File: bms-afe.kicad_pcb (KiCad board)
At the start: 0 parts

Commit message: started layout
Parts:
- added C11: CAP CER 1000PF 50V X7R 0603, Capacitor_SMD:C_0603_1608Metric, F.Cu at (121.5, 115.4)
- added C12: CAP CER 1000PF 50V X7R 0603, Capacitor_SMD:C_0603_1608Metric, F.Cu at (149.8, 106.7)
- added C13: CAP CER 1000PF 50V X7R 0603, Capacitor_SMD:C_0603_1608Metric, F.Cu at (121.5, 117.9)
- added C14: CAP CER 250PF 25V NP0 0603, Capacitor_SMD:C_0603_1608Metric, F.Cu at (203.0, 42.0)
- added C15: CAP CER 0603 1NF 16V X7R 10%, Capacitor_SMD:C_0603_1608Metric, F.Cu at (200.5, 45.0)
- added C16: CAP CER 220PF 50V X7R 0603, Capacitor_SMD:C_0603_1608Metric, F.Cu at (202.5, 45.0)
- added C17: CAP CER 0603 1NF 16V X7R 10%, Capacitor_SMD:C_0603_1608Metric, F.Cu at (208.0, 41.5)
- added C18: 4.7nF, Capacitor_SMD:C_0603_1608Metric, F.Cu at (166.1, 39.8)
- added C19: CAP CER 220PF 50V X7R 0603, Capacitor_SMD:C_0603_1608Metric, F.Cu at (210.0, 41.5)
- added C20: 4.7nF, Capacitor_SMD:C_0603_1608Metric, F.Cu at (166.1, 44.8)
- added C21: 4.7nF, Capacitor_SMD:C_0603_1608Metric, F.Cu at (170.1, 29.8)
- added C22: 1000pF, Capacitor_SMD:C_0603_1608Metric, F.Cu at (170.1, 32.3)
- added C23: CAP CER 220PF 50V X7R 0603, Capacitor_SMD:C_0603_1608Metric, F.Cu at (198.5, 48.0)
- added C24: CAP CER 0603 1NF 16V X7R 10%, Capacitor_SMD:C_0603_1608Metric, F.Cu at (196.5, 48.0)
- added C25: 10nF, Capacitor_SMD:C_0603_1608Metric, F.Cu at (170.1, 39.8)
- added C26: CAP CER 1000PF 50V X7R 0603, Capacitor_SMD:C_0603_1608Metric, F.Cu at (165.0, 76.8)
- added C27: CAP CER 220PF 50V X7R 0603, Capacitor_SMD:C_0603_1608Metric, F.Cu at (194.0, 46.0)
- added C28: CAP CER 0603 1NF 16V X7R 10%, Capacitor_SMD:C_0603_1608Metric, F.Cu at (194.0, 44.0)
- added C29: 10nF, Capacitor_SMD:C_0603_1608Metric, F.Cu at (174.1, 29.8)
- added C30: 10nF, Capacitor_SMD:C_0603_1608Metric, F.Cu at (174.1, 32.3)
- added C31: CAP CER 1000PF 50V X7R 0603, Capacitor_SMD:C_0603_1608Metric, F.Cu at (149.8, 76.8)
- added C32: CAP CER 1000PF 50V X7R 0603, Capacitor_SMD:C_0603_1608Metric, F.Cu at (149.8, 121.6)
- added C33: CAP CER 1000PF 50V X7R 0603, Capacitor_SMD:C_0603_1608Metric, F.Cu at (149.8, 91.7)
- added C34: CAP CER 1000PF 50V X7R 0603, Capacitor_SMD:C_0603_1608Metric, F.Cu at (165.0, 91.7)
- added C35: CAP CER 0.1UF 25V X7R 0603, Capacitor_SMD:C_0603_1608Metric, F.Cu at (149.8, 109.2)
- added C37: CAP CER 0.1UF 25V X7R 0603, Capacitor_SMD:C_0603_1608Metric, F.Cu at (165.0, 79.3)
- added C39: CAP CER 0.1UF 25V X7R 0603, Capacitor_SMD:C_0603_1608Metric, F.Cu at (149.8, 79.3)
- added C41: CAP CER 0.1UF 25V X7R 0603, Capacitor_SMD:C_0603_1608Metric, F.Cu at (149.8, 124.1)
- added C42: CAP CER 0.1UF 25V X7R 0603, Capacitor_SMD:C_0603_1608Metric, F.Cu at (149.8, 94.2)
- added C43: CAP CER 0.1UF 25V X7R 0603, Capacitor_SMD:C_0603_1608Metric, F.Cu at (165.0, 94.2)
- added C44: 0.1uF, Capacitor_SMD:C_0603_1608Metric, F.Cu at (203.0, 34.0)
- added C45: 0.1uF, Capacitor_SMD:C_0603_1608Metric, F.Cu at (203.0, 38.0)
- added C46: 0.1uF, Capacitor_SMD:C_0603_1608Metric, F.Cu at (203.0, 36.0)
- added C47: 0.1uF, Capacitor_SMD:C_0603_1608Metric, F.Cu at (186.0, 47.5)
- added C54: CAP CER 0.33UF 16V X7R 0603, Capacitor_SMD:C_0603_1608Metric, F.Cu at (121.5, 120.5)
- added C55: CAP CER 0.33UF 16V X7R 0603, Capacitor_SMD:C_0603_1608Metric, F.Cu at (121.5, 123.0)
- added C56: CAP CER 0.33UF 16V X7R 0603, Capacitor_SMD:C_0603_1608Metric, F.Cu at (125.5, 115.4)
- added C57: CAP CER 0.33UF 16V X7R 0603, Capacitor_SMD:C_0603_1608Metric, F.Cu at (125.5, 117.9)
- added C58: CAP CER 0.33UF 16V X7R 0603, Capacitor_SMD:C_0603_1608Metric, F.Cu at (125.5, 120.5)
- added C59: CAP CER 0.33UF 16V X7R 0603, Capacitor_SMD:C_0603_1608Metric, F.Cu at (125.5, 123.0)
- added C60: CAP CER 0.33UF 25V X7R 0603, Capacitor_SMD:C_0603_1608Metric, F.Cu at (129.5, 115.4)
- added D1: 1.6X0.8MM RED/WHT SMD LED, Diode_SMD:D_0603_1608Metric, F.Cu at (159.0, 115.2)
- added D2: 1.6X0.8MM RED/WHT SMD LED, Diode_SMD:D_0603_1608Metric, F.Cu at (174.2, 85.3)
- added D3: 1.6X0.8MM RED/WHT SMD LED, Diode_SMD:D_0603_1608Metric, F.Cu at (159.0, 85.3)
- added D4: 1.6X0.8MM RED/WHT SMD LED, Diode_SMD:D_0603_1608Metric, F.Cu at (159.0, 130.1)
- added D5: 1.6X0.8MM RED/WHT SMD LED, Diode_SMD:D_0603_1608Metric, F.Cu at (159.0, 100.2)
- added D6: 1.6X0.8MM RED/WHT SMD LED, Diode_SMD:D_0603_1608Metric, F.Cu at (174.2, 100.2)
- added GSF1: MOSFET, P-CH, SINGLE, -4.1A, -30, Package_TO_SOT_SMD:SOT-23-3, F.Cu at (154.4, 116.1)
- added GSF2: MOSFET, P-CH, SINGLE, -4.1A, -30, Package_TO_SOT_SMD:SOT-23-3, F.Cu at (169.6, 86.2)
- added GSF3: MOSFET, P-CH, SINGLE, -4.1A, -30, Package_TO_SOT_SMD:SOT-23-3, F.Cu at (154.4, 86.2)
- added GSF4: MOSFET, P-CH, SINGLE, -4.1A, -30, Package_TO_SOT_SMD:SOT-23-3, F.Cu at (154.4, 131.1)
- added GSF5: MOSFET, P-CH, SINGLE, -4.1A, -30, Package_TO_SOT_SMD:SOT-23-3, F.Cu at (154.4, 101.2)
- added GSF6: MOSFET, P-CH, SINGLE, -4.1A, -30, Package_TO_SOT_SMD:SOT-23-3, F.Cu at (169.6, 101.2)
- added J1: CONN HEADER VERT 7POS 2.5MM, footprints:JST_B7B-XH-A_LF__SN_, F.Cu at (71.0, 99.5)
- added J2: CONN HEADER VERT 2POS 1.5MM, footprints:CONN_B2B-ZR_02P_JST, F.Cu at (191.0, 89.5)
- added J3: CONN HEADER VERT 2POS 1.5MM, footprints:CONN_B2B-ZR_02P_JST, F.Cu at (207.0, 87.5)
- added J4: CONN HEADER VERT 6POS 1.5MM, footprints:CONN_B6B-ZR_JST, F.Cu at (168.6, 49.1)
- added R1: RES 10 OHM 1% 1/10W 0603, Resistor_SMD:R_0603_1608Metric, F.Cu at (129.5, 117.9)
- added R10: RES SMD 52.3 OHM 1% 1/2W 1210, Capacitor_SMD:C_1210_3225Metric, F.Cu at (169.9, 77.6)
- added R11: RES SMD 52.3 OHM 1% 1/2W 1210, Capacitor_SMD:C_1210_3225Metric, F.Cu at (169.9, 81.9)
- added R12: RES SMD 8.2 OHM 1% 1/8W 0603, Capacitor_SMD:C_0603_1608Metric, F.Cu at (165.0, 81.8)
- added R13: RES 10 OHM 1% 1/10W 0603, Resistor_SMD:R_0603_1608Metric, F.Cu at (165.0, 84.3)
- added R14: RES 100 OHM 1% 1/10W 0603, Resistor_SMD:R_0603_1608Metric, F.Cu at (200.5, 41.5)
- added R15: 100, Resistor_SMD:R_0603_1608Metric, F.Cu at (203.0, 40.0)
- added R16: 20k, Capacitor_SMD:C_0603_1608Metric, F.Cu at (216.0, 38.5)
- added R17: 20k, Capacitor_SMD:C_0603_1608Metric, F.Cu at (216.0, 41.0)
- added R18: RES SMD 39 OHM 5% 1/8W 0603, Resistor_SMD:R_0603_1608Metric, F.Cu at (198.5, 43.0)
- added R19: 20k, Capacitor_SMD:C_0603_1608Metric, F.Cu at (178.1, 39.8)
- added R2: RES 10 OHM 1% 1/10W 0603, Resistor_SMD:R_0603_1608Metric, F.Cu at (129.5, 120.5)
- added R20: 20k, Capacitor_SMD:C_0603_1608Metric, F.Cu at (178.1, 42.3)
- added R21: RES SMD 39 OHM 5% 1/8W 0603, Resistor_SMD:R_0603_1608Metric, F.Cu at (206.0, 40.0)
- added R22: RES 100 OHM 1% 1/10W 0603, Resistor_SMD:R_0603_1608Metric, F.Cu at (182.1, 29.8)
- added R23: RES SMD 10K OHM 1% 1/8W 0603, Resistor_SMD:R_0603_1608Metric, F.Cu at (182.1, 32.3)
- added R24: RES SMD 39 OHM 5% 1/8W 0603, Resistor_SMD:R_0603_1608Metric, F.Cu at (198.0, 45.5)
- added R25: RES SMD 10K OHM 1% 1/8W 0603, Resistor_SMD:R_0603_1608Metric, F.Cu at (182.1, 37.3)
- added R26: RES SMD 39 OHM 5% 1/8W 0603, Resistor_SMD:R_0603_1608Metric, F.Cu at (196.5, 43.0)
- added R27: 10, Resistor_SMD:R_0603_1608Metric, F.Cu at (182.1, 42.3)
- added R28: 5.1, Resistor_SMD:R_0603_1608Metric, F.Cu at (186.1, 45.8)
- added R29: RES SMD 52.3 OHM 1% 1/2W 1210, Capacitor_SMD:C_1210_3225Metric, F.Cu at (154.7, 77.6)
- added R3: RES SMD 5.1 OHM 1% 1/8W 0603, Resistor_SMD:R_0603_1608Metric, F.Cu at (129.5, 123.0)
- added R30: RES SMD 52.3 OHM 1% 1/2W 1210, Capacitor_SMD:C_1210_3225Metric, F.Cu at (154.7, 81.9)
- added R31: RES SMD 8.2 OHM 1% 1/8W 0603, Capacitor_SMD:C_0603_1608Metric, F.Cu at (149.8, 81.8)
- added R32: RES 10 OHM 1% 1/10W 0603, Resistor_SMD:R_0603_1608Metric, F.Cu at (149.8, 84.3)
- added R33: RES SMD 52.3 OHM 1% 1/2W 1210, Capacitor_SMD:C_1210_3225Metric, F.Cu at (154.7, 122.5)
- added R34: RES SMD 52.3 OHM 1% 1/2W 1210, Capacitor_SMD:C_1210_3225Metric, F.Cu at (154.7, 126.7)
- added R35: RES SMD 8.2 OHM 1% 1/8W 0603, Capacitor_SMD:C_0603_1608Metric, F.Cu at (149.8, 126.6)
- added R36: RES 10 OHM 1% 1/10W 0603, Resistor_SMD:R_0603_1608Metric, F.Cu at (149.8, 129.1)
- added R37: RES SMD 52.3 OHM 1% 1/2W 1210, Capacitor_SMD:C_1210_3225Metric, F.Cu at (154.7, 92.6)
- added R38: RES SMD 52.3 OHM 1% 1/2W 1210, Capacitor_SMD:C_1210_3225Metric, F.Cu at (154.7, 96.8)
- added R39: RES SMD 8.2 OHM 1% 1/8W 0603, Capacitor_SMD:C_0603_1608Metric, F.Cu at (149.8, 96.7)
- added R4: 0, Resistor_SMD:R_0603_1608Metric, F.Cu at (202.0, 84.0)
- added R40: RES 10 OHM 1% 1/10W 0603, Resistor_SMD:R_0603_1608Metric, F.Cu at (149.8, 99.2)
- added R41: RES SMD 52.3 OHM 1% 1/2W 1210, Capacitor_SMD:C_1210_3225Metric, F.Cu at (169.9, 92.6)
- added R42: RES SMD 52.3 OHM 1% 1/2W 1210, Capacitor_SMD:C_1210_3225Metric, F.Cu at (169.9, 96.8)
- added R43: RES SMD 8.2 OHM 1% 1/8W 0603, Capacitor_SMD:C_0603_1608Metric, F.Cu at (165.0, 96.7)
- added R44: RES 10 OHM 1% 1/10W 0603, Resistor_SMD:R_0603_1608Metric, F.Cu at (165.0, 99.2)
- added R45: RES SMD 487 OHM 1% 1/10W 0603, Capacitor_SMD:C_0603_1608Metric, F.Cu at (149.8, 116.7)
- added R46: RES SMD 487 OHM 1% 1/10W 0603, Capacitor_SMD:C_0603_1608Metric, F.Cu at (165.0, 86.8)
- added R47: RES SMD 487 OHM 1% 1/10W 0603, Capacitor_SMD:C_0603_1608Metric, F.Cu at (149.8, 86.8)
- added R48: RES SMD 487 OHM 1% 1/10W 0603, Capacitor_SMD:C_0603_1608Metric, F.Cu at (149.8, 131.6)
- added R49: RES SMD 487 OHM 1% 1/10W 0603, Capacitor_SMD:C_0603_1608Metric, F.Cu at (149.8, 101.7)
- added R5: 0, Resistor_SMD:R_0603_1608Metric, F.Cu at (202.0, 92.8)
- added R50: RES SMD 487 OHM 1% 1/10W 0603, Capacitor_SMD:C_0603_1608Metric, F.Cu at (165.0, 101.7)
- added R51: RES SMD 1K OHM 0.1% 1/10W 0603, Resistor_SMD:R_0603_1608Metric, F.Cu at (199.0, 88.5)
- added R6: RES SMD 52.3 OHM 1% 1/2W 1210, Capacitor_SMD:C_1210_3225Metric, F.Cu at (154.7, 107.5)
- added R7: RES SMD 52.3 OHM 1% 1/2W 1210, Capacitor_SMD:C_1210_3225Metric, F.Cu at (154.7, 111.8)
- added R8: RES SMD 8.2 OHM 1% 1/8W 0603, Capacitor_SMD:C_0603_1608Metric, F.Cu at (149.8, 111.7)
- added R9: RES 10 OHM 1% 1/10W 0603, Resistor_SMD:R_0603_1608Metric, F.Cu at (149.8, 114.2)
- added T1: PULSE XFMR 15UH 1 OHM FOR PLC, footprints:AMT45S-150-2P-TL000, F.Cu at (200.4, 85.0)
- added U1: TLE9012DQUXUMA1, footprints:PG-TQFP-48-9, F.Cu at (196.0, 36.0)
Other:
- copper layers 0 -> 2

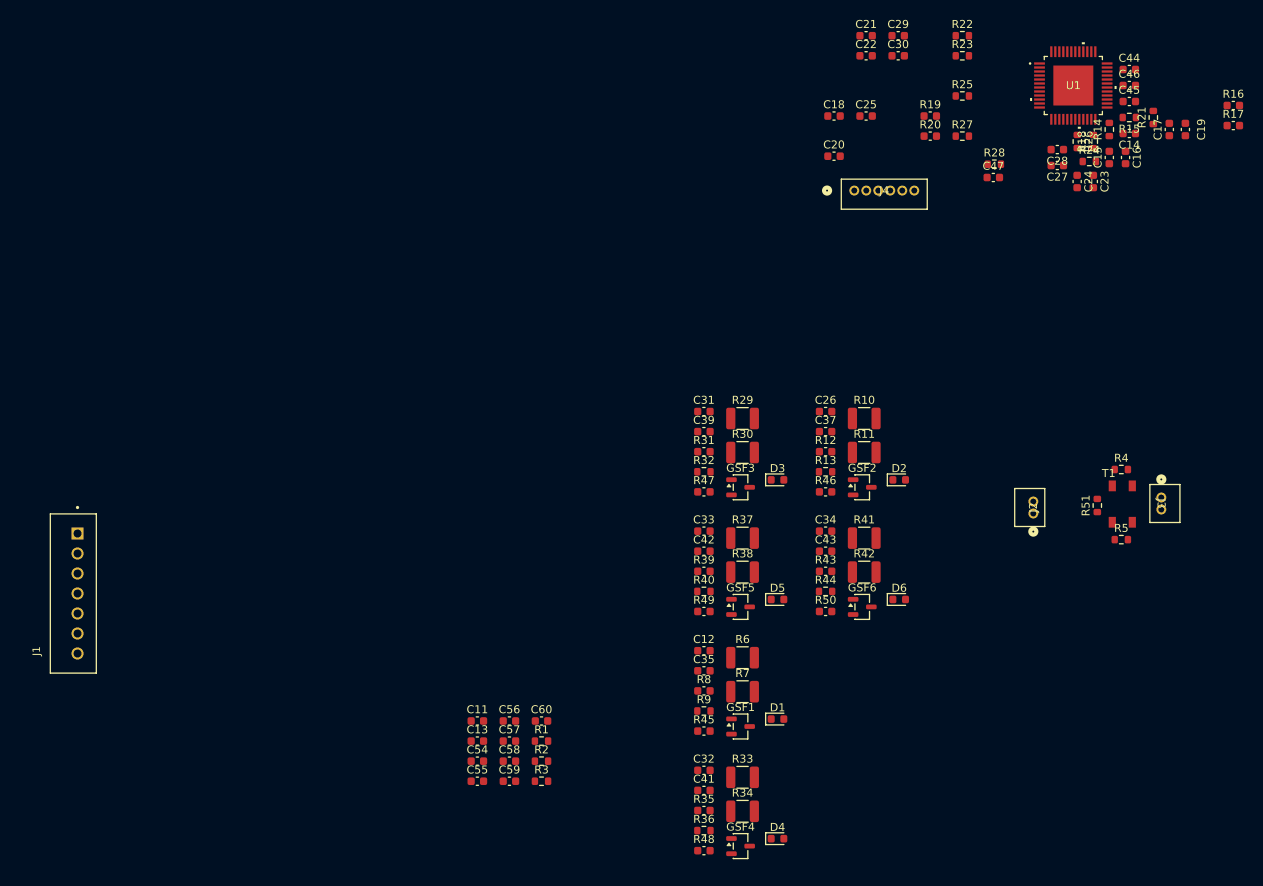
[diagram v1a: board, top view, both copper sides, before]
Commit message: initial component layout
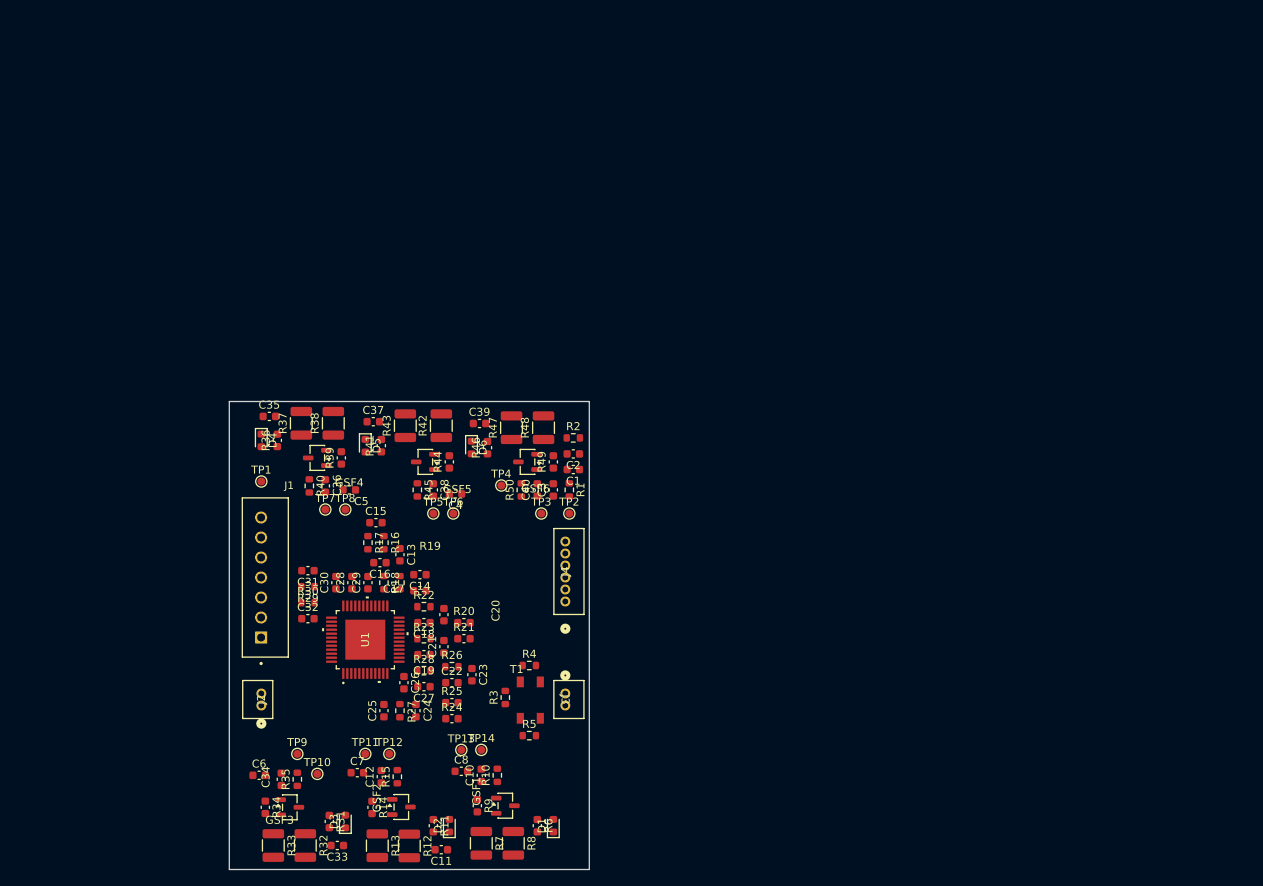
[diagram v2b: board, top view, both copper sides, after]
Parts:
- removed C41, C42, C43: CAP CER 0.1UF 25V X7R 0603, Capacitor_SMD:C_0603_1608Metric
- removed C44, C45, C46, C47: 0.1uF, Capacitor_SMD:C_0603_1608Metric
- removed C54, C55, C56, C57, C58, C59: CAP CER 0.33UF 16V X7R 0603, Capacitor_SMD:C_0603_1608Metric
- removed C60: CAP CER 0.33UF 25V X7R 0603, Capacitor_SMD:C_0603_1608Metric
- removed R51: RES SMD 1K OHM 0.1% 1/10W 0603, Resistor_SMD:R_0603_1608Metric
- added C1: CAP CER 1000PF 50V X7R 0603, Capacitor_SMD:C_0603_1608Metric, F.Cu at (133.5, 84.0)
- added C10: CAP CER 0.1UF 25V X7R 0603, Capacitor_SMD:C_0603_1608Metric, F.Cu at (122.0, 122.2)
- added C2: CAP CER 1000PF 50V X7R 0603, Capacitor_SMD:C_0603_1608Metric, F.Cu at (133.5, 82.0)
- added C3: CAP CER 0.33UF 16V X7R 0603, Capacitor_SMD:C_0603_1608Metric, F.Cu at (131.0, 86.5)
- added C36: CAP CER 0.1UF 25V X7R 0603, Capacitor_SMD:C_0603_1608Metric, F.Cu at (102.5, 86.0)
- added C38: CAP CER 0.1UF 25V X7R 0603, Capacitor_SMD:C_0603_1608Metric, F.Cu at (116.0, 86.5)
- added C4: CAP CER 0.33UF 16V X7R 0603, Capacitor_SMD:C_0603_1608Metric, F.Cu at (118.8, 87.0)
- added C40: CAP CER 0.1UF 25V X7R 0603, Capacitor_SMD:C_0603_1608Metric, F.Cu at (129.0, 86.5)
- added C5: CAP CER 0.33UF 16V X7R 0603, Capacitor_SMD:C_0603_1608Metric, F.Cu at (105.5, 86.5)
- added C6: CAP CER 0.33UF 16V X7R 0603, Capacitor_SMD:C_0603_1608Metric, F.Cu at (94.2, 122.2)
- added C7: CAP CER 0.33UF 16V X7R 0603, Capacitor_SMD:C_0603_1608Metric, F.Cu at (106.5, 121.9)
- added C8: CAP CER 0.33UF 16V X7R 0603, Capacitor_SMD:C_0603_1608Metric, F.Cu at (119.5, 121.7)
- added TP1: TestPoint, TestPoint:TestPoint_Pad_D1.0mm, F.Cu at (94.5, 85.5)
- added TP10: TestPoint, TestPoint:TestPoint_Pad_D1.0mm, F.Cu at (101.5, 122.0)
- added TP11: TestPoint, TestPoint:TestPoint_Pad_D1.0mm, F.Cu at (107.5, 119.5)
- added TP12: TestPoint, TestPoint:TestPoint_Pad_D1.0mm, F.Cu at (110.5, 119.5)
- added TP13: TestPoint, TestPoint:TestPoint_Pad_D1.0mm, F.Cu at (119.5, 119.0)
- added TP14: TestPoint, TestPoint:TestPoint_Pad_D1.0mm, F.Cu at (122.0, 119.0)
- added TP2: TestPoint, TestPoint:TestPoint_Pad_D1.0mm, F.Cu at (133.0, 89.5)
- added TP3: TestPoint, TestPoint:TestPoint_Pad_D1.0mm, F.Cu at (129.5, 89.5)
- added TP4: TestPoint, TestPoint:TestPoint_Pad_D1.0mm, F.Cu at (124.5, 86.0)
- added TP5: TestPoint, TestPoint:TestPoint_Pad_D1.0mm, F.Cu at (116.0, 89.5)
- added TP6: TestPoint, TestPoint:TestPoint_Pad_D1.0mm, F.Cu at (118.5, 89.5)
- added TP7: TestPoint, TestPoint:TestPoint_Pad_D1.0mm, F.Cu at (102.5, 89.0)
- added TP8: TestPoint, TestPoint:TestPoint_Pad_D1.0mm, F.Cu at (105.0, 89.0)
- added TP9: TestPoint, TestPoint:TestPoint_Pad_D1.0mm, F.Cu at (99.0, 119.5)
- C12, C34: value CAP CER 1000PF 50V X7R 0603 -> CAP CER 0.1UF 25V X7R 0603
- C13: value CAP CER 1000PF 50V X7R 0603 -> CAP CER 0603 1NF 16V X7R 10%
- C14: value CAP CER 250PF 25V NP0 0603 -> CAP CER 0603 1NF 16V X7R 10%
- C15: value CAP CER 0603 1NF 16V X7R 10% -> CAP CER 250PF 25V NP0 0603
- C17: value CAP CER 0603 1NF 16V X7R 10% -> CAP CER 220PF 50V X7R 0603
- C18: value 4.7nF -> CAP CER 220PF 50V X7R 0603
- C20, C21: value 4.7nF -> CAP CER 0603 1NF 16V X7R 10%
- C22: value 1000pF -> 10nF
- C23, C27: value CAP CER 220PF 50V X7R 0603 -> 4.7nF
- C24: value CAP CER 0603 1NF 16V X7R 10% -> 10nF
- C25: value 10nF -> 4.7nF
- C26: value CAP CER 1000PF 50V X7R 0603 -> 10nF
- C28: value CAP CER 0603 1NF 16V X7R 10% -> 0.1uF
- C29: value 10nF -> 0.33uF
- C30: value 10nF -> 100nF
- C31: value CAP CER 1000PF 50V X7R 0603 -> 1nF
- C32: value CAP CER 1000PF 50V X7R 0603 -> 100nF
- C35, C37, C39: value CAP CER 0.1UF 25V X7R 0603 -> CAP CER 1000PF 50V X7R 0603
- R10: value RES SMD 52.3 OHM 1% 1/2W 1210 -> RES 10 OHM 1% 1/10W 0603; footprint Capacitor_SMD:C_1210_3225Metric -> Resistor_SMD:R_0603_1608Metric
- R11, R41, R6: value RES SMD 52.3 OHM 1% 1/2W 1210 -> RES SMD 487 OHM 1% 1/10W 0603; footprint Capacitor_SMD:C_1210_3225Metric -> Capacitor_SMD:C_0603_1608Metric
- R12, R43, R8: value RES SMD 8.2 OHM 1% 1/8W 0603 -> RES SMD 52.3 OHM 1% 1/2W 1210; footprint Capacitor_SMD:C_0603_1608Metric -> Capacitor_SMD:C_1210_3225Metric
- R13, R32: value RES 10 OHM 1% 1/10W 0603 -> RES SMD 52.3 OHM 1% 1/2W 1210; footprint Resistor_SMD:R_0603_1608Metric -> Capacitor_SMD:C_1210_3225Metric
- R14: value RES 100 OHM 1% 1/10W 0603 -> RES SMD 8.2 OHM 1% 1/8W 0603; footprint Resistor_SMD:R_0603_1608Metric -> Capacitor_SMD:C_0603_1608Metric
- R15: value 100 -> RES 10 OHM 1% 1/10W 0603
- R16: value 20k -> RES 100 OHM 1% 1/10W 0603; footprint Capacitor_SMD:C_0603_1608Metric -> Resistor_SMD:R_0603_1608Metric
- R17: value 20k -> 100; footprint Capacitor_SMD:C_0603_1608Metric -> Resistor_SMD:R_0603_1608Metric
- R19: value 20k -> RES SMD 39 OHM 5% 1/8W 0603; footprint Capacitor_SMD:C_0603_1608Metric -> Resistor_SMD:R_0603_1608Metric
- R2: value RES 10 OHM 1% 1/10W 0603 -> RES SMD 5.1 OHM 1% 1/8W 0603
- R21, R24: value RES SMD 39 OHM 5% 1/8W 0603 -> 20k; footprint Resistor_SMD:R_0603_1608Metric -> Capacitor_SMD:C_0603_1608Metric
- R22: value RES 100 OHM 1% 1/10W 0603 -> RES SMD 39 OHM 5% 1/8W 0603
- R23: value RES SMD 10K OHM 1% 1/8W 0603 -> RES SMD 39 OHM 5% 1/8W 0603
- R25: value RES SMD 10K OHM 1% 1/8W 0603 -> 20k; footprint Resistor_SMD:R_0603_1608Metric -> Capacitor_SMD:C_0603_1608Metric
- R26: value RES SMD 39 OHM 5% 1/8W 0603 -> RES 100 OHM 1% 1/10W 0603
- R27: value 10 -> RES SMD 10K OHM 1% 1/8W 0603
- R28: value 5.1 -> RES SMD 10K OHM 1% 1/8W 0603
- R29: value RES SMD 52.3 OHM 1% 1/2W 1210 -> 10; footprint Capacitor_SMD:C_1210_3225Metric -> Resistor_SMD:R_0603_1608Metric
- R3: value RES SMD 5.1 OHM 1% 1/8W 0603 -> RES SMD 1K OHM 0.1% 1/10W 0603
- R30: value RES SMD 52.3 OHM 1% 1/2W 1210 -> 5.1; footprint Capacitor_SMD:C_1210_3225Metric -> Resistor_SMD:R_0603_1608Metric
- R31: value RES SMD 8.2 OHM 1% 1/8W 0603 -> RES SMD 487 OHM 1% 1/10W 0603
- R34: value RES SMD 52.3 OHM 1% 1/2W 1210 -> RES SMD 8.2 OHM 1% 1/8W 0603; footprint Capacitor_SMD:C_1210_3225Metric -> Capacitor_SMD:C_0603_1608Metric
- R35: value RES SMD 8.2 OHM 1% 1/8W 0603 -> RES 10 OHM 1% 1/10W 0603; footprint Capacitor_SMD:C_0603_1608Metric -> Resistor_SMD:R_0603_1608Metric
- R36: value RES 10 OHM 1% 1/10W 0603 -> RES SMD 487 OHM 1% 1/10W 0603; footprint Resistor_SMD:R_0603_1608Metric -> Capacitor_SMD:C_0603_1608Metric
- R44, R9: value RES 10 OHM 1% 1/10W 0603 -> RES SMD 8.2 OHM 1% 1/8W 0603; footprint Resistor_SMD:R_0603_1608Metric -> Capacitor_SMD:C_0603_1608Metric
- R45, R50: value RES SMD 487 OHM 1% 1/10W 0603 -> RES 10 OHM 1% 1/10W 0603; footprint Capacitor_SMD:C_0603_1608Metric -> Resistor_SMD:R_0603_1608Metric
- R47, R48: value RES SMD 487 OHM 1% 1/10W 0603 -> RES SMD 52.3 OHM 1% 1/2W 1210; footprint Capacitor_SMD:C_0603_1608Metric -> Capacitor_SMD:C_1210_3225Metric
- R49: value RES SMD 487 OHM 1% 1/10W 0603 -> RES SMD 8.2 OHM 1% 1/8W 0603
- moved R14 125.2 mm to (108.3, 126.2), turned to -90 degrees
- moved R15 123.1 mm to (111.5, 122.4), turned to 90 degrees
- moved R17 120.1 mm to (107.8, 93.1), turned to -90 degrees
- moved R16 119.4 mm to (109.8, 93.1), turned to -90 degrees
- moved C19 115.6 mm to (114.8, 107.1), turned to 180 degrees
- moved U1 112.4 mm to (107.5, 105.3), turned to 90 degrees
- moved C17 110.0 mm to (114.3, 99.1), turned to 0 degrees
- moved R21 108.0 mm to (119.8, 105.1), turned to 0 degrees
- moved C16 106.1 mm to (109.3, 95.6), turned to 180 degrees
- moved C24 105.9 mm to (113.8, 114.1)
- moved R24 105.8 mm to (118.3, 115.1)
- moved C14 104.4 mm to (114.3, 97.1)
- moved R18 104.4 mm to (109.8, 98.1), turned to -90 degrees
- moved C28 103.5 mm to (105.8, 98.1), turned to 90 degrees
- moved C27 102.5 mm to (114.8, 111.1)
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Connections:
- C11 pad 2: /CellBalance5/Battery_Pos -> /CellBalance/Battery_Pos
- C12 pad 1: BATGND -> /AFEIC/G1
- C12 pad 2: BATGND -> /AFEIC/U1
- C13 pad 1: BATGND -> /AFEIC/IFH_L
- C13 pad 2: /CellBalance5/Battery_Pos -> Net-(C13-Pad2)
- C14 pad 1: Net-(C14-Pad1) -> /AFEIC/IFH_H
- C15 pad 1: /AFEIC/IFH_H -> Net-(C15-Pad1)
- C16 pad 1: Net-(C15-Pad2) -> Net-(C13-Pad2)
- C17 pad 1: /AFEIC/IFH_L -> Net-(C14-Pad2)
- C17 pad 2: Net-(C17-Pad2) -> BATGND
- C18 pad 1: /AFEIC/TMP2 -> Net-(C18-Pad1)
- C19 pad 1: Net-(C17-Pad2) -> Net-(C19-Pad1)
- C19 pad 2: BATGND -> BAT_GND
- C20 pad 1: /AFEIC/TMP1 -> Net-(C18-Pad1)
- C20 pad 2: BATGND -> /AFEIC/IFL_H
- C21 pad 1: /AFEIC/TMP0 -> Net-(C19-Pad1)
- C21 pad 2: BATGND -> /AFEIC/IFL_L
- C22 pad 1: /AFEIC/U12P -> Net-(U1A-TMP2)
- C23 pad 1: Net-(C23-Pad1) -> /AFEIC/TMP2
- C24 pad 1: Net-(C23-Pad1) -> Net-(U1A-TMP1)
- C24 pad 2: /AFEIC/IFL_H -> BATGND
- C25 pad 1: Net-(U1A-TMP0) -> /AFEIC/TMP1
- C26 pad 1: BATGND -> Net-(U1A-TMP0)
- C26 pad 2: /CellBalance/Battery_Pos -> BATGND
- C27 pad 1: Net-(C27-Pad1) -> /AFEIC/TMP0
- C27 pad 2: BAT_GND -> BATGND
- C28 pad 1: Net-(C27-Pad1) -> VBLK
- C28 pad 2: /AFEIC/IFL_L -> BATGND
- C29 pad 1: Net-(U1A-TMP2) -> Net-(U1B-VDDC)
- C30 pad 1: Net-(U1A-TMP1) -> /AFEIC/VREGOUT
- C31 pad 1: BATGND -> /AFEIC/U12P
- C31 pad 2: /CellBalance1/Battery_Pos -> BATGND
- C32 pad 1: BATGND -> Net-(C32-Pad1)
- C32 pad 2: /CellBalance2/Battery_Pos -> BATGND
- C33 pad 2: /CellBalance3/Battery_Pos -> /CellBalance1/Battery_Pos
- C34 pad 1: BATGND -> /AFEIC/G2
- C34 pad 2: /CellBalance4/Battery_Pos -> /AFEIC/U2
- C35 pad 1: /AFEIC/G0 -> BATGND
- C35 pad 2: /AFEIC/U0 -> /CellBalance2/Battery_Pos
- C37 pad 1: /AFEIC/G1 -> BATGND
- C37 pad 2: /AFEIC/U1 -> /CellBalance3/Battery_Pos
- C39 pad 1: /AFEIC/G2 -> BATGND
- C39 pad 2: /AFEIC/U2 -> /CellBalance4/Battery_Pos
- GSF6 pad 2: /CellBalance5/Battery_Pos -> /AFEIC/U12P
- J1 pad 7: /CellBalance5/Battery_Pos -> /AFEIC/U12P
- R1 pad 1: /CellBalance5/Battery_Pos -> /AFEIC/U12P
- R1 pad 2: VBLK -> /AFEIC/U6
- R10 pad 1: Net-(GSF2-D) -> BATGND
- R10 pad 2: /CellBalance/Battery_Pos -> /AFEIC/U0
- R11 pad 1: Net-(GSF2-D) -> Net-(D2-A)
- R11 pad 2: /CellBalance/Battery_Pos -> Net-(GSF2-D)
- R12 pad 1: /AFEIC/G1 -> Net-(GSF2-D)
- R12 pad 2: /CellBalance1/Battery_Pos -> /CellBalance/Battery_Pos
- R13 pad 1: /CellBalance/Battery_Pos -> Net-(GSF2-D)
- R13 pad 2: /AFEIC/U1 -> /CellBalance/Battery_Pos
- R14 pad 1: Net-(C14-Pad2) -> /AFEIC/G1
- R14 pad 2: /AFEIC/IFH_H_Filt -> /CellBalance1/Battery_Pos
- R15 pad 1: Net-(C14-Pad1) -> /CellBalance/Battery_Pos
- R15 pad 2: /AFEIC/IFH_L_Filt -> /AFEIC/U1
- R16 pad 1: Net-(U1A-PWM0) -> Net-(C15-Pad2)
- R16 pad 2: BATGND -> /AFEIC/IFH_H_Filt
- R17 pad 1: Net-(U1A-PWM1) -> Net-(C15-Pad1)
- R17 pad 2: BATGND -> /AFEIC/IFH_L_Filt
- R18 pad 1: Net-(C15-Pad2) -> Net-(C13-Pad2)
- R18 pad 2: /AFEIC/IFH_H_Filt -> /AFEIC/IFH_L_Filt
- R19 pad 1: Net-(U1A-TMP4) -> Net-(C14-Pad2)
- R19 pad 2: BATGND -> /AFEIC/IFH_H_Filt
- R2 pad 1: /CellBalance5/Battery_Pos -> /AFEIC/U12P
- R2 pad 2: /AFEIC/U6 -> VBLK
- R20 pad 1: Net-(U1A-TMP3) -> Net-(U1A-PWM0)
- R21 pad 1: Net-(C17-Pad2) -> Net-(U1A-PWM1)
- R21 pad 2: /AFEIC/IFH_L_Filt -> BATGND
- R22 pad 1: Net-(U1A-TMP2) -> /AFEIC/IFL_H_Filt
- R22 pad 2: /AFEIC/TMP2 -> Net-(C18-Pad1)
- R23 pad 1: Net-(U1A-TMP1) -> /AFEIC/IFL_L_Filt
- R23 pad 2: /AFEIC/TMP1 -> Net-(C19-Pad1)
- R24 pad 1: /AFEIC/IFL_H_Filt -> Net-(U1A-TMP4)
- R24 pad 2: Net-(C23-Pad1) -> BATGND
- R25 pad 1: Net-(U1A-TMP0) -> Net-(U1A-TMP3)
- R25 pad 2: /AFEIC/TMP0 -> BATGND
- R26 pad 1: /AFEIC/IFL_L_Filt -> Net-(U1A-TMP2)
- R26 pad 2: Net-(C27-Pad1) -> /AFEIC/TMP2
- R27 pad 1: /AFEIC/U12P -> Net-(U1A-TMP1)
- R27 pad 2: Net-(C47-Pad1) -> /AFEIC/TMP1
- R28 pad 1: Net-(C47-Pad1) -> Net-(U1A-TMP0)
- R28 pad 2: Net-(U1B-U12P) -> /AFEIC/TMP0
- R29 pad 1: Net-(GSF3-D) -> /AFEIC/U12P
- R29 pad 2: /CellBalance1/Battery_Pos -> Net-(C32-Pad1)
- R3 pad 1: VBLK -> /AFEIC/IFL_L
- R3 pad 2: /AFEIC/U12P -> /AFEIC/IFL_H
- R30 pad 1: Net-(GSF3-D) -> Net-(C32-Pad1)
- R30 pad 2: /CellBalance1/Battery_Pos -> Net-(U1B-U12P)
- R31 pad 1: /AFEIC/G2 -> Net-(D3-A)
- R31 pad 2: /CellBalance2/Battery_Pos -> Net-(GSF3-D)
- R32 pad 1: /CellBalance1/Battery_Pos -> Net-(GSF3-D)
- R32 pad 2: /AFEIC/U2 -> /CellBalance1/Battery_Pos
- R33 pad 1: Net-(GSF4-D) -> Net-(GSF3-D)
- R33 pad 2: /CellBalance2/Battery_Pos -> /CellBalance1/Battery_Pos
- R34 pad 1: Net-(GSF4-D) -> /AFEIC/G2
- R35 pad 1: /AFEIC/G3 -> /CellBalance1/Battery_Pos
- R35 pad 2: /CellBalance3/Battery_Pos -> /AFEIC/U2
- R36 pad 1: /CellBalance2/Battery_Pos -> Net-(D4-A)
- R36 pad 2: /AFEIC/U3 -> Net-(GSF4-D)
- R37 pad 1: Net-(GSF5-D) -> Net-(GSF4-D)
- R37 pad 2: /CellBalance3/Battery_Pos -> /CellBalance2/Battery_Pos
- R38 pad 1: Net-(GSF5-D) -> Net-(GSF4-D)
- R38 pad 2: /CellBalance3/Battery_Pos -> /CellBalance2/Battery_Pos
- R39 pad 1: /AFEIC/G4 -> /AFEIC/G3
- R39 pad 2: /CellBalance4/Battery_Pos -> /CellBalance3/Battery_Pos
- R40 pad 1: /CellBalance3/Battery_Pos -> /CellBalance2/Battery_Pos
- R40 pad 2: /AFEIC/U4 -> /AFEIC/U3
- R41 pad 1: Net-(GSF6-D) -> Net-(D5-A)
- R41 pad 2: /CellBalance4/Battery_Pos -> Net-(GSF5-D)
- R42 pad 1: Net-(GSF6-D) -> Net-(GSF5-D)
- R42 pad 2: /CellBalance4/Battery_Pos -> /CellBalance3/Battery_Pos
- R43 pad 1: /AFEIC/G5 -> Net-(GSF5-D)
- R43 pad 2: /CellBalance5/Battery_Pos -> /CellBalance3/Battery_Pos
- R44 pad 1: /CellBalance4/Battery_Pos -> /AFEIC/G4
- R44 pad 2: /AFEIC/U5 -> /CellBalance4/Battery_Pos
- R45 pad 1: Net-(D1-A) -> /CellBalance3/Battery_Pos
- R45 pad 2: Net-(GSF1-D) -> /AFEIC/U4
- R46 pad 1: Net-(D2-A) -> Net-(D6-A)
- R46 pad 2: Net-(GSF2-D) -> Net-(GSF6-D)
- R47 pad 1: Net-(D3-A) -> Net-(GSF6-D)
- R47 pad 2: Net-(GSF3-D) -> /CellBalance4/Battery_Pos
- R48 pad 1: Net-(D4-A) -> Net-(GSF6-D)
- R48 pad 2: Net-(GSF4-D) -> /CellBalance4/Battery_Pos
- R49 pad 1: Net-(D5-A) -> /AFEIC/G5
- R49 pad 2: Net-(GSF5-D) -> /AFEIC/U12P
- R50 pad 1: Net-(D6-A) -> /CellBalance4/Battery_Pos
- R50 pad 2: Net-(GSF6-D) -> /AFEIC/U5
- R6 pad 1: Net-(GSF1-D) -> Net-(D1-A)
- R6 pad 2: BATGND -> Net-(GSF1-D)
- R8 pad 1: /AFEIC/G0 -> Net-(GSF1-D)
- R8 pad 2: /CellBalance/Battery_Pos -> BATGND
- R9 pad 1: BATGND -> /AFEIC/G0
- R9 pad 2: /AFEIC/U0 -> /CellBalance/Battery_Pos
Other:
- board outline added: 45 x 58.5 mm

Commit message: first layout
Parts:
- C15, C22, C23, C24, C25, C26, C27, R16, R17, R20, R21, R24, R25, R26, R27, R28: moved to B.Cu
- moved C2 74.7 mm to (67.4, 116.8), turned to 0 degrees
- moved R48 74.2 mm to (68.7, 120.9), turned to -90 degrees
- moved C1 72.9 mm to (67.4, 114.8), turned to 0 degrees
- moved R2 72.6 mm to (68.2, 111.8), turned to 90 degrees
- moved R1 71.3 mm to (66.3, 111.8), turned to 90 degrees
- moved R49 69.1 mm to (70.0, 115.5), turned to -90 degrees
- moved R47 67.8 mm to (72.7, 120.9), turned to -90 degrees
- moved TP2 65.9 mm to (70.0, 108.7), turned to 180 degrees
- moved C3 65.0 mm to (70.7, 110.9), turned to 0 degrees
- moved GSF6 64.3 mm to (72.6, 116.1), turned to -90 degrees
- moved C40 63.9 mm to (70.7, 112.8), turned to 0 degrees
- moved C39 63.6 mm to (75.4, 121.7), turned to 90 degrees
- moved TP3 60.1 mm to (72.5, 108.7), turned to 180 degrees
- moved R50 59.3 mm to (73.4, 112.0), turned to -90 degrees
- moved D6 58.5 mm to (75.4, 118.2), turned to 90 degrees
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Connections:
- C19 pad 2: BAT_GND -> BATGND
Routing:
- net /AFEIC/U12P: track 0.00 -> 65.4 mm, vias 0 -> 2
- net /CellBalance4/Battery_Pos: track 0.00 -> 46.1 mm, vias 0 -> 2
- net BATGND: track 0.00 -> 45.6 mm, vias 0 -> 14
- net /CellBalance3/Battery_Pos: track 0.00 -> 39.6 mm, vias 0 -> 2
- net /AFEIC/TMP1: track 0.00 -> 35.1 mm
- net /CellBalance/Battery_Pos: track 0.00 -> 34.4 mm, vias 0 -> 2
- net /CellBalance2/Battery_Pos: track 0.00 -> 34.3 mm, vias 0 -> 2
- net /AFEIC/G5: track 0.00 -> 33.2 mm
- net /AFEIC/G0: track 0.00 -> 32.4 mm
- net /CellBalance1/Battery_Pos: track 0.00 -> 31.7 mm, vias 0 -> 2
- net VBLK: track 0.00 -> 31.7 mm, vias 0 -> 2
- net /AFEIC/U0: track 0.00 -> 29.9 mm
- net /AFEIC/U6: track 0.00 -> 28.8 mm
- net /AFEIC/U1: track 0.00 -> 28.4 mm, vias 0 -> 2
- net /AFEIC/U5: track 0.00 -> 26.3 mm, vias 0 -> 2
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- added copper zone on B.Cu, net BATGND
- added copper zone on F.Cu, net BATGND
- added copper zone on F.Cu, net Net-(GSF1-D)
- added copper zone on F.Cu, net Net-(GSF2-D)
- added copper zone on F.Cu, net Net-(GSF3-D)
- added copper zone on F.Cu, net Net-(GSF4-D)
- added copper zone on F.Cu, net Net-(GSF5-D)
- added copper zone on F.Cu, net Net-(GSF6-D)
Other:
- board size 45 x 58.5 mm -> 60.3 x 37.9 mm

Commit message: fixed minor layout changes
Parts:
- moved C20 0.56 mm to (104.9, 100.5)
- moved R3 0.41 mm to (115.2, 104.4)
- moved C21 0.36 mm to (104.9, 104.1)
- moved R18 0.32 mm to (97.5, 97.3)
- moved R21 0.30 mm to (103.2, 105.1)
- moved C30 0.25 mm to (93.6, 97.3)
- moved C29 0.22 mm to (95.4, 97.3)
- moved TP12 0.20 mm to (115.3, 111.1)
- moved C28 0.16 mm to (91.7, 97.3)
- moved R19 0.12 mm to (99.3, 97.3)
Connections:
- net /AFEIC/IFH_H renamed /AFEIC/IFH_P
- net /AFEIC/IFH_H_Filt renamed /AFEIC/IFH_Filt_P
- net /AFEIC/IFH_L renamed /AFEIC/IFH_N
- net /AFEIC/IFH_L_Filt renamed /AFEIC/IFH_Filt_N
- net /AFEIC/IFL_H renamed /AFEIC/IFL_P
- net /AFEIC/IFL_L renamed /AFEIC/IFL_N
- R22 pad 1: /AFEIC/IFL_H_Filt -> /AFEIC/IFL_Filt_P
- R23 pad 1: /AFEIC/IFL_L_Filt -> /AFEIC/IFL_Filt_N
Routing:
- net BATGND: track 45.6 -> 37.0 mm, vias 14 -> 13
- net /AFEIC/TMP0: track 23.2 -> 20.2 mm
- net Net-(U1A-TMP0): track 9.33 -> 6.94 mm
- net /AFEIC/IFL_N: track 16.3 -> 18.0 mm
- net Net-(U1A-TMP4): track 10.5 -> 11.6 mm
- net Net-(C15-Pad1): track 2.88 -> 1.75 mm, vias 1 -> 0
- net /AFEIC/IFL_P: track 17.2 -> 18.2 mm
- net Net-(C18-Pad1): track 3.77 -> 4.38 mm

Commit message: minor layout changes
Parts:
- added IFHN: TestPoint, TestPoint:TestPoint_Pad_D1.0mm, F.Cu at (109.8, 94.8)
- added IFHP: TestPoint, TestPoint:TestPoint_Pad_D1.0mm, F.Cu at (109.8, 96.9)
- added IFLN: TestPoint, TestPoint:TestPoint_Pad_D1.0mm, F.Cu at (122.6, 108.0)
- added IFLP: TestPoint, TestPoint:TestPoint_Pad_D1.0mm, F.Cu at (122.6, 100.4)
- moved J4 2.27 mm to (120.7, 96.3)
- moved R20 0.64 mm to (102.7, 102.6)
- moved C19 0.50 mm to (102.3, 104.7)
- moved R21 0.40 mm to (103.2, 104.7)
- moved TP1 0.14 mm to (84.2, 127.6), turned to 0 degrees
- renumbered TP14 to G0, TP11 to G1, TP9 to G2, TP7 to G3, TP5 to G4, TP3 to G5, TP13 to U0, TP12 to U1, GSF1 to U1, TP10 to U2, GSF2 to U3, TP8 to U3, GSF3 to U4, TP6 to U4, GSF4 to U5, TP4 to U5, GSF5 to U6, TP2 to U6, GSF6 to U7, U1 to U8
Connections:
- U8 pad 23: /AFEIC/IFL_L_Filt -> /AFEIC/IFL_Filt_N
- U8 pad 24: /AFEIC/IFL_H_Filt -> /AFEIC/IFL_Filt_P
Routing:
- net BATGND: track 37.0 -> 42.3 mm, vias 13 -> 12
- net /AFEIC/IFH_P: track 3.93 -> 7.96 mm
- net /AFEIC/IFH_N: track 4.09 -> 8.02 mm
- net /AFEIC/IFL_H_Filt: track 3.75 -> 0.00 mm
- net /AFEIC/IFL_Filt_P: track 0.00 -> 3.75 mm
- net /AFEIC/U12P: track 65.4 -> 61.8 mm, vias 2 -> 3
- net /AFEIC/TMP2: track 17.0 -> 20.3 mm
- net Net-(J3-Pad1): track 5.92 -> 9.12 mm
- net /AFEIC/IFL_L_Filt: track 3.19 -> 0.00 mm
- net /AFEIC/IFL_Filt_N: track 0.00 -> 3.19 mm
- net Net-(J3-Pad2): track 6.18 -> 9.18 mm
- net /AFEIC/TMP0: track 20.2 -> 22.5 mm
- net /AFEIC/TMP1: track 35.1 -> 37.3 mm
- net /AFEIC/U6: track 28.8 -> 27.6 mm
- net Net-(U8A-TMP0): track 6.94 -> 8.12 mm
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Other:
- board text added: "BMS AFE"
- board text added: "Bat Monitor"
- board text added: "Eleanor W"
- board text added: "TEMP CONN"
- board text added: "UP"

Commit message: damir review fix
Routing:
- net BATGND: vias 12 -> 99
